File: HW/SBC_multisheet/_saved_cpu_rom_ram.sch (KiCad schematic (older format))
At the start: 3 parts, among them U1 WD65C02_, U2 28C256, U3 HM62256BLP-7

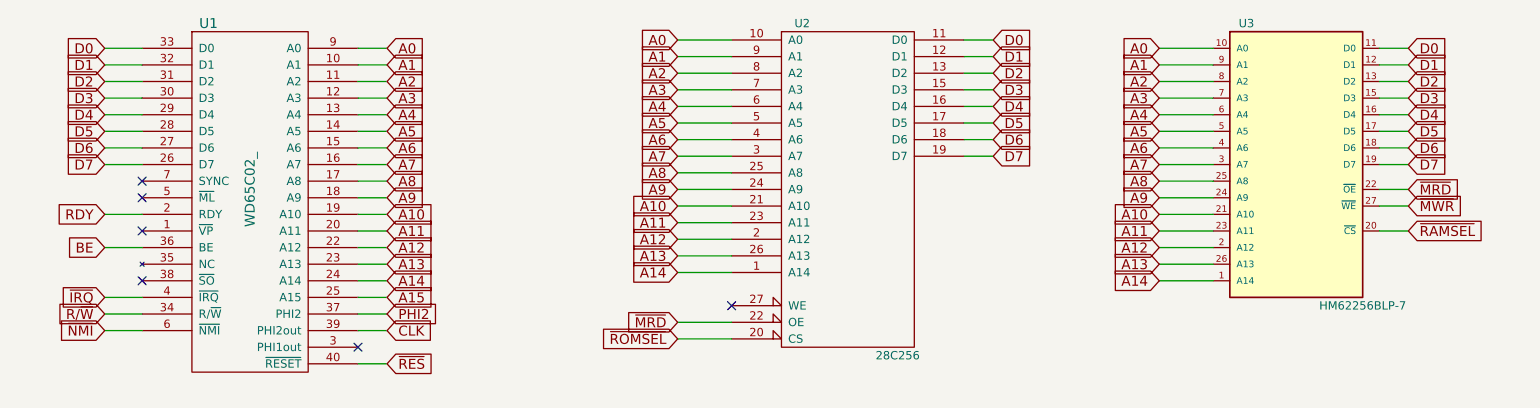
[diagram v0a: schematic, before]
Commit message: The PCB layout editor doesn't like 7805's footprint.
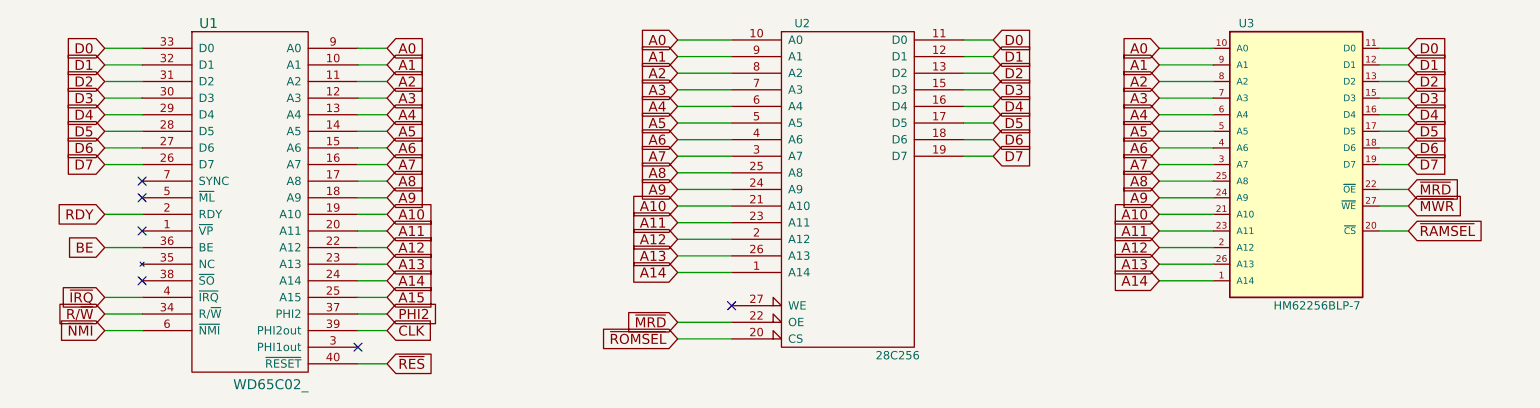
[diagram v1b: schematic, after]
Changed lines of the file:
@@
 P 2175 2350
 F 0 "U1" H 1925 3400 60  0000 C CNN
-F 1 "WD65C02_" V 2175 2400 60  0000 C CNN
+F 1 "WD65C02_" H 2300 1225 60  0000 C CNN
 F 2 "Housings_DIP:DIP-40_W15.24mm" H 1625 2550 60  0001 C CNN
 F 3 "" H 1625 2550 60  0000 C CNN
@@
 P 8475 2200
 F 0 "U3" H 8175 3100 50  0000 C CNN
-F 1 "HM62256BLP-7" H 8875 1400 50  0000 C CNN
+F 1 "HM62256BLP-7" H 8600 1400 50  0000 C CNN
 F 2 "Housings_DIP:DIP-28_W15.24mm" H 8475 2200 50  0001 C CIN
 F 3 "" H 8475 2200 50  0001 C CNN
